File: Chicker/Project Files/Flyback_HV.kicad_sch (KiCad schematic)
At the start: 56 parts, among them Q2 IRFR3410TRPBF_alternate, Q3 FGH50T65SQD-F155, Q7 FGH50T65SQD-F155, T1 DA2034, U2 MCP14A0454-E/SN_alternate, U4 LT3750

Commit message: changing file locations
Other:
- note added: "Technically the transformer is inverted, but it works electrically and likely does not cause an excess current leakage for the dot being on the wrong side."

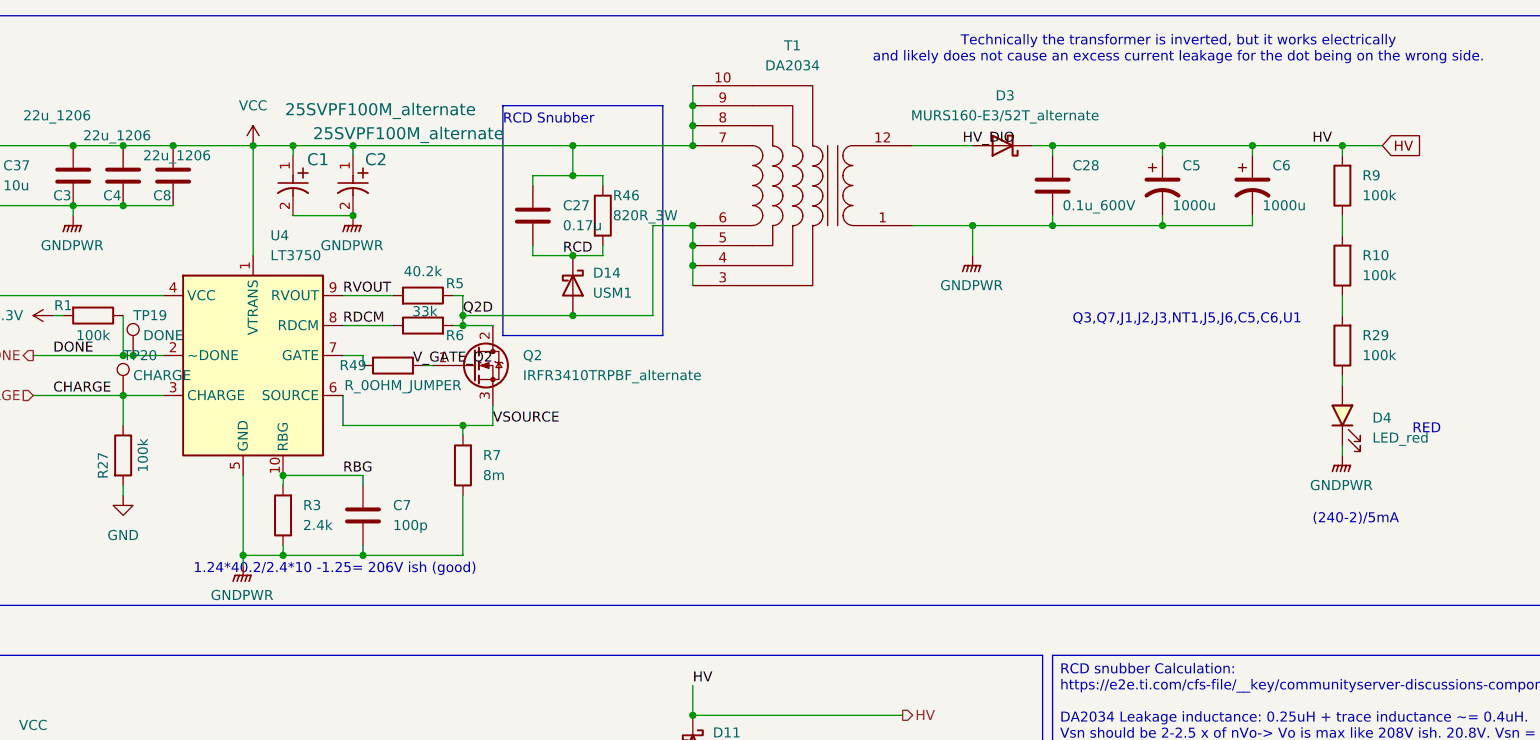
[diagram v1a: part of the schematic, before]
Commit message: fix text on schematic
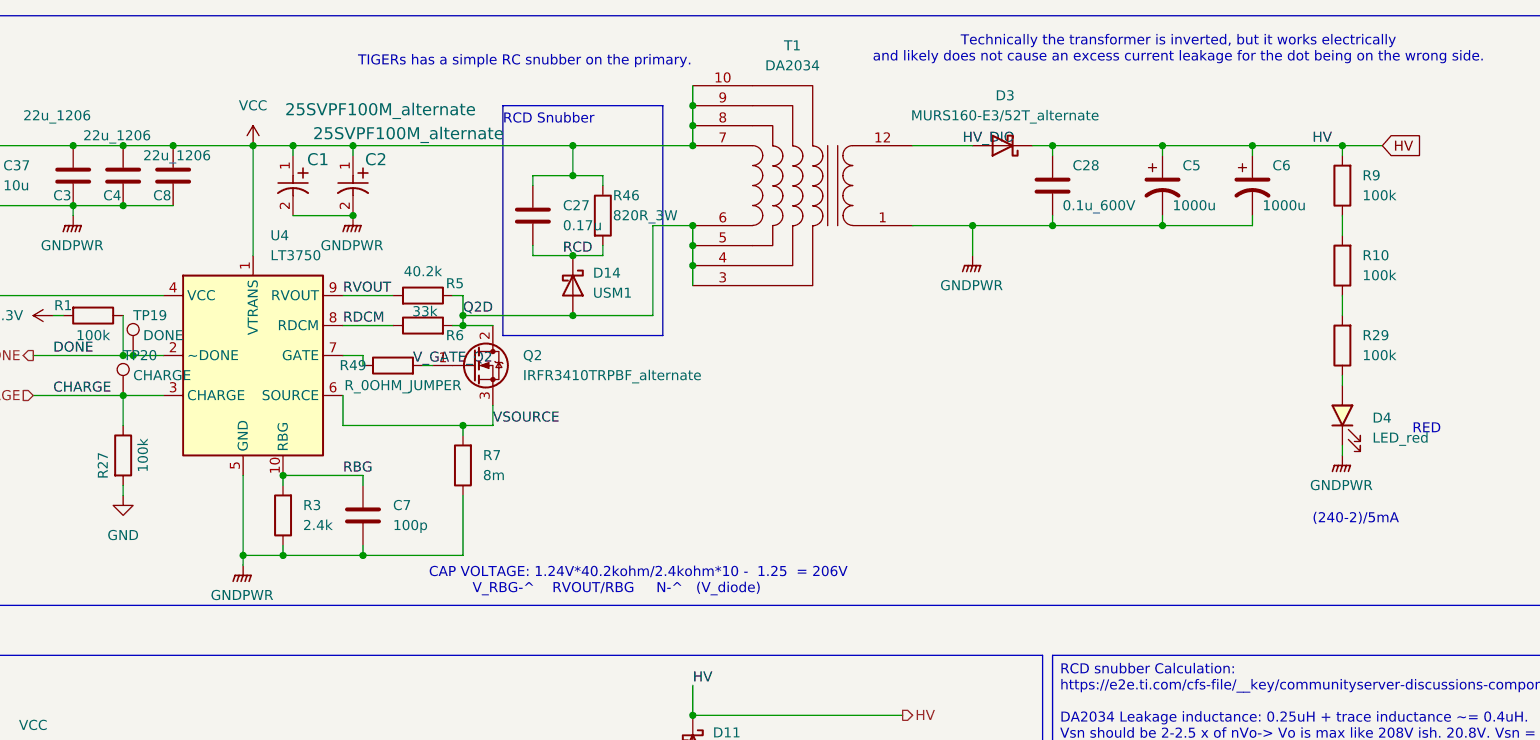
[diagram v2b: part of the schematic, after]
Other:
- note added: "CAP VOLTAGE: 1.24V*40.2kohm/2.4kohm*10 - 1.25 = 206V V_RBG-^ RVOUT/RBG N-^ (V_diode)"
- note added: "TIGERs has a simple RC snubber on the primary."
- note removed: "1.24*40.2/2.4*10 -1.25= 206V ish (good)"
- note removed: "Q3,Q7,J1,J2,J3,NT1,J5,J6,C5,C6,U1"

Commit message: libraries and stuff
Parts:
- R49: value R_0OHM_JUMPER -> 0R
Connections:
- net DONE is gone; now on net VCC: R1.1, TP19.1, U4.2 (~DONE)
- net V_GATE_Q2: now also Q2.1 (G), R49.2
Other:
- note added: "Coss = Cds + Cgd = 92pF Crss = Cgd = 90pF Ciss = Cgs + Cgd = 1500pF, Rg = 1.5ohms (maximum, worst case values)"
- note added: "Lleak = Ll_transformer + Ll_parasitic"
- moved on the sheet: C7, R1, R27, R3, R49, R5, R6, R7, TP19, TP20, U4
